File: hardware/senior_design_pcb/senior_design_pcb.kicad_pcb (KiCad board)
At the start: 4 copper layers, 15 parts, among them J8 Conn_02x08_Odd_Even, SW2 SW_Push, U1 FT232RL, U2 STM32F091RCTx, U3 LD1117S33TR_SOT223, X1 32.768kHz(12.5pF), X2 8MHz(20pF)

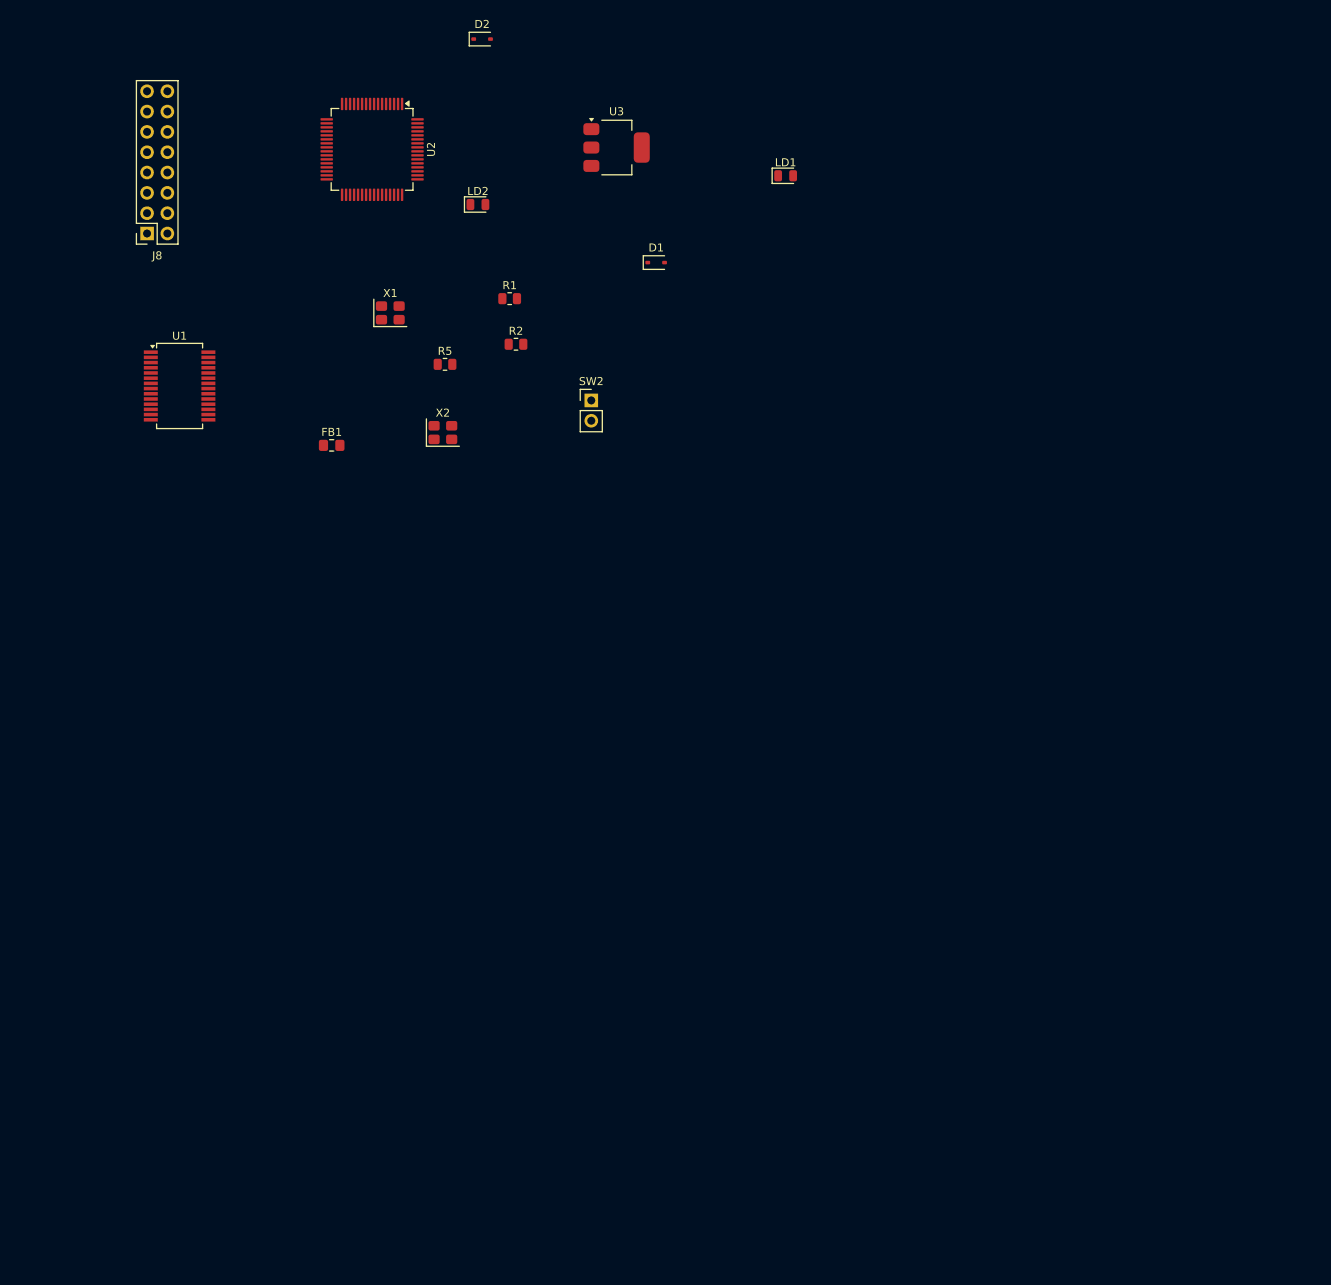
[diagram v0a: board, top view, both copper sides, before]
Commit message: added pcb, removed schematic level
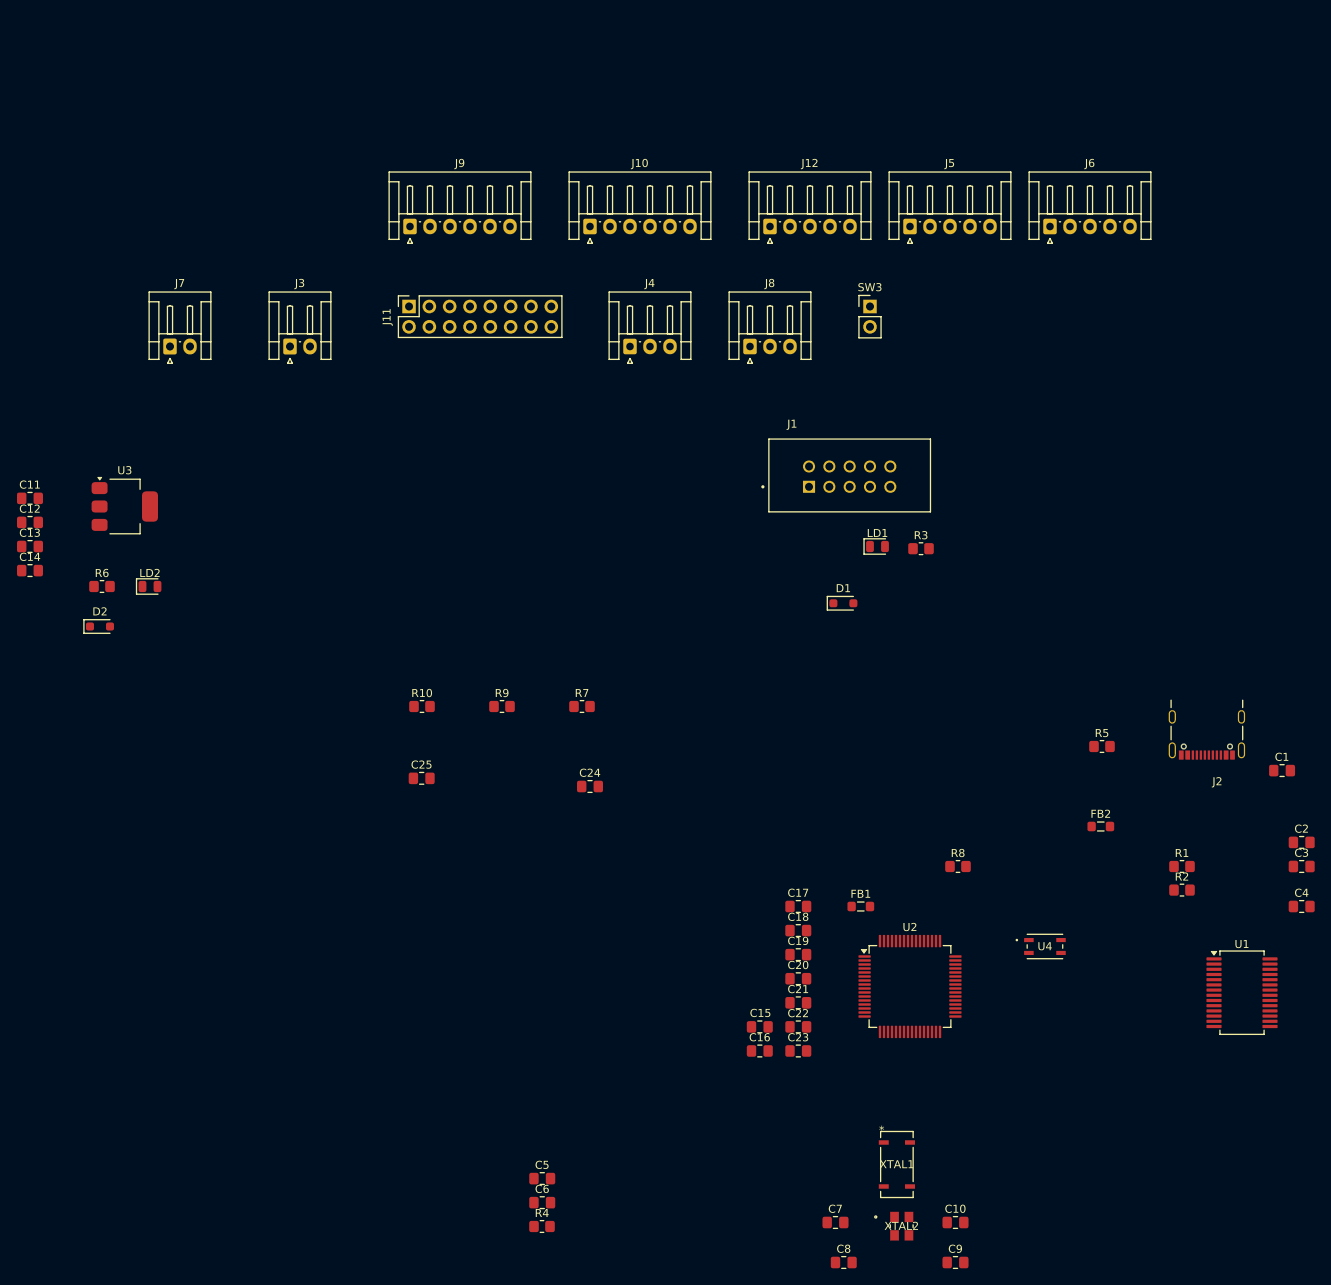
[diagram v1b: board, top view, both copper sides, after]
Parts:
- removed SW2: SW_Push, Connector_PinHeader_2.54mm:PinHeader_1x02_P2.54mm_Vertical
- removed X1: 32.768kHz(12.5pF), Crystal:Crystal_SMD_3225-4Pin_3.2x2.5mm
- removed X2: 8MHz(20pF), Crystal:Crystal_SMD_3225-4Pin_3.2x2.5mm
- added C1: 10nF, Capacitor_SMD:C_0805_2012Metric_Pad1.18x1.45mm_HandSolder, F.Cu at (191.5, 128.0)
- added C10: 22uF, Capacitor_SMD:C_0805_2012Metric_Pad1.18x1.45mm_HandSolder, F.Cu at (150.7, 184.5)
- added C11: .1uF, Capacitor_SMD:C_0805_2012Metric_Pad1.18x1.45mm_HandSolder, F.Cu at (35.0, 94.0)
- added C12: .1uF, Capacitor_SMD:C_0805_2012Metric_Pad1.18x1.45mm_HandSolder, F.Cu at (35.0, 97.0)
- added C13: .1uF, Capacitor_SMD:C_0805_2012Metric_Pad1.18x1.45mm_HandSolder, F.Cu at (35.0, 100.0)
- added C14: 4.7uf, Capacitor_SMD:C_0805_2012Metric_Pad1.18x1.45mm_HandSolder, F.Cu at (35.0, 103.0)
- added C15: .1uF, Capacitor_SMD:C_0805_2012Metric_Pad1.18x1.45mm_HandSolder, F.Cu at (126.2, 160.1)
- added C16: 4.7uf, Capacitor_SMD:C_0805_2012Metric_Pad1.18x1.45mm_HandSolder, F.Cu at (126.2, 163.1)
- added C17: 1uf, Capacitor_SMD:C_0805_2012Metric_Pad1.18x1.45mm_HandSolder, F.Cu at (131.0, 145.0)
- added C18: 10nf, Capacitor_SMD:C_0805_2012Metric_Pad1.18x1.45mm_HandSolder, F.Cu at (131.0, 148.0)
- added C19: 1uf, Capacitor_SMD:C_0805_2012Metric_Pad1.18x1.45mm_HandSolder, F.Cu at (131.0, 151.0)
- added C2: 100nF, Capacitor_SMD:C_0805_2012Metric_Pad1.18x1.45mm_HandSolder, F.Cu at (194.0, 137.0)
- added C20: 12.5pF, Capacitor_SMD:C_0805_2012Metric_Pad1.18x1.45mm_HandSolder, F.Cu at (131.0, 154.0)
- added C21: 12.5pF, Capacitor_SMD:C_0805_2012Metric_Pad1.18x1.45mm_HandSolder, F.Cu at (131.0, 157.0)
- added C22: .1uF, Capacitor_SMD:C_0805_2012Metric_Pad1.18x1.45mm_HandSolder, F.Cu at (131.0, 160.1)
- added C23: .1uF, Capacitor_SMD:C_0805_2012Metric_Pad1.18x1.45mm_HandSolder, F.Cu at (131.0, 163.1)
- added C24: .1uF, Capacitor_SMD:C_0805_2012Metric_Pad1.18x1.45mm_HandSolder, F.Cu at (105.0, 130.0)
- added C25: .1uF, Capacitor_SMD:C_0805_2012Metric_Pad1.18x1.45mm_HandSolder, F.Cu at (84.0, 129.0)
- added C3: 4.7uF, Capacitor_SMD:C_0805_2012Metric_Pad1.18x1.45mm_HandSolder, F.Cu at (194.0, 140.0)
- added C4: 100nF, Capacitor_SMD:C_0805_2012Metric_Pad1.18x1.45mm_HandSolder, F.Cu at (194.0, 145.0)
- added C5: 20pF, Capacitor_SMD:C_0805_2012Metric_Pad1.18x1.45mm_HandSolder, F.Cu at (99.0, 179.0)
- added C6: 20pF, Capacitor_SMD:C_0805_2012Metric_Pad1.18x1.45mm_HandSolder, F.Cu at (99.0, 182.0)
- added C7: 22uF, Capacitor_SMD:C_0805_2012Metric_Pad1.18x1.45mm_HandSolder, F.Cu at (135.7, 184.5)
- added C8: .1uF, Capacitor_SMD:C_0805_2012Metric_Pad1.18x1.45mm_HandSolder, F.Cu at (136.7, 189.5)
- added C9: .1uF, Capacitor_SMD:C_0805_2012Metric_Pad1.18x1.45mm_HandSolder, F.Cu at (150.7, 189.5)
- added FB2: Ferrite Bead, Inductor_SMD:L_0805_2012Metric_Pad1.05x1.20mm_HandSolder, F.Cu at (168.8, 135.0)
- added J1: SBH11-PBPC-D05-ST-BK, General Library:jtag_conn, F.Cu at (137.5, 91.3)
- added J10: Screw_Terminal_01x06, Connector_JST:JST_EH_S6B-EH_1x06_P2.50mm_Horizontal, F.Cu at (105.0, 60.0)
- added J11: Conn_02x08_Odd_Even, Connector_PinSocket_2.54mm:PinSocket_2x08_P2.54mm_Vertical, F.Cu at (82.4, 70.0)
- added J12: Conn_01x05_Socket, Connector_JST:JST_EH_S5B-EH_1x05_P2.50mm_Horizontal, F.Cu at (127.5, 60.0)
- added J2: USB_C_Receptacle_USB2.0_16P, Sr_ Design:USB-C-PORT-2, F.Cu at (182.1, 122.3)
- added J3: Conn_01x02_Socket, Connector_JST:JST_EH_S2B-EH_1x02_P2.50mm_Horizontal, F.Cu at (67.5, 75.0)
- added J4: Conn_01x03_Socket, Connector_JST:JST_EH_S3B-EH_1x03_P2.50mm_Horizontal, F.Cu at (110.0, 75.0)
- added J5: Conn_01x05_Socket, Connector_JST:JST_EH_S5B-EH_1x05_P2.50mm_Horizontal, F.Cu at (145.0, 60.0)
- added J6: Conn_01x05_Socket, Connector_JST:JST_EH_S5B-EH_1x05_P2.50mm_Horizontal, F.Cu at (162.5, 60.0)
- added J7: Conn_01x02_Socket, Connector_JST:JST_EH_S2B-EH_1x02_P2.50mm_Horizontal, F.Cu at (52.5, 75.0)
- added J9: Screw_Terminal_01x06, Connector_JST:JST_EH_S6B-EH_1x06_P2.50mm_Horizontal, F.Cu at (82.5, 60.0)
- added R10: 10K, Resistor_SMD:R_0805_2012Metric_Pad1.20x1.40mm_HandSolder, F.Cu at (84.0, 120.0)
- added R3: 5k11, Resistor_SMD:R_0805_2012Metric_Pad1.20x1.40mm_HandSolder, F.Cu at (146.4, 100.3)
- added R4: 1M, Resistor_SMD:R_0805_2012Metric_Pad1.20x1.40mm_HandSolder, F.Cu at (99.0, 185.0)
- added R6: 10K, Resistor_SMD:R_0805_2012Metric_Pad1.20x1.40mm_HandSolder, F.Cu at (44.0, 105.0)
- added R7: 100K, Resistor_SMD:R_0805_2012Metric_Pad1.20x1.40mm_HandSolder, F.Cu at (104.0, 120.0)
- added R8: 10K, Resistor_SMD:R_0805_2012Metric_Pad1.20x1.40mm_HandSolder, F.Cu at (151.0, 140.0)
- added R9: 10K, Resistor_SMD:R_0805_2012Metric_Pad1.20x1.40mm_HandSolder, F.Cu at (94.0, 120.0)
- added SW3: SW_Push, Connector_PinHeader_2.54mm:PinHeader_1x02_P2.54mm_Vertical, F.Cu at (140.0, 70.0)
- added U4: KMR241GLFS, General Library:KMR241G-RESET-BUTTON, F.Cu at (161.9, 150.0)
- added XTAL1: 32.768kHz(12.5pF), Sr_ Design:ECS - CRYSTAL 32.7680KHZ 6PF SMD, F.Cu at (143.4, 177.2)
- added XTAL2: 8MHz(8PF), Sr_ Design:ECS-CRYSTAL 8MHZ 8PF SMD, F.Cu at (144.0, 185.0)
- D1, D2: footprint Diode_SMD:D_SOD-323 -> Diode_SMD:D_SOD-323_HandSoldering
- FB1: footprint Inductor_SMD:L_0805_2012Metric_Pad1.15x1.40mm_HandSolder -> Inductor_SMD:L_0805_2012Metric_Pad1.05x1.20mm_HandSolder
- J8: value Conn_02x08_Odd_Even -> Conn_01x03_Socket; footprint Connector_PinSocket_2.54mm:PinSocket_2x08_P2.54mm_Vertical -> Connector_JST:JST_EH_S3B-EH_1x03_P2.50mm_Horizontal
- R1, R2: footprint Resistor_SMD:R_0805_2012Metric -> Resistor_SMD:R_0805_2012Metric_Pad1.20x1.40mm_HandSolder
- R5: value 1M -> 1k; footprint Resistor_SMD:R_0805_2012Metric -> Resistor_SMD:R_0805_2012Metric_Pad1.20x1.40mm_HandSolder
- moved U1 152.9 mm to (186.5, 155.8)
- moved U2 124.4 mm to (145.0, 155.0), turned to 0 degrees
- moved R1 110.0 mm to (179.0, 140.0)
- moved R2 107.6 mm to (179.0, 142.9)
- moved R5 95.0 mm to (169.0, 125.0)
- moved FB1 87.7 mm to (138.8, 145.0)
- moved D2 87.6 mm to (43.8, 110.0)
- moved J8 76.7 mm to (125.0, 75.0), turned to 0 degrees
- moved U3 76.1 mm to (46.9, 95.0)
- moved LD2 62.9 mm to (50.0, 105.0)
- moved D1 48.6 mm to (136.7, 107.1)
- moved LD1 47.7 mm to (140.9, 100.0)
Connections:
- net /stm/PC13 renamed /stm/CONTROLLER-BUTTON
- FB1 pad 1: /stm/3VA -> +5V
- FB1 pad 2: +3V0 -> /stm/VBUS
- J8 pad 1: /stm/PB11 -> +5V
- J8 pad 2: /stm/G1 -> /stm/IR_IN_2
- J8 pad 3: /stm/B1 -> GND
- R5 pad 1: Net-(J2-SHIELD) -> +3V0
- R5 pad 2: GND -> Net-(LD2-A)
- U2 pad 10: /stm/PC2 -> /stm/ADMIN_JOYSTICK-BUTTON
- U2 pad 43: /stm/ADMIN_JOYSTICK-BUTTON -> /stm/PA10
- U2 pad 44: /stm/ADMIN_JOYSTICK-Y -> /stm/PA11
- U2 pad 45: /stm/ADMIN_JOYSTICK-X -> /stm/PA12
- U2 pad 8: /stm/PC0 -> /stm/ADMIN_JOYSTICK-X
- U2 pad 9: /stm/PC1 -> /stm/ADMIN_JOYSTICK-Y
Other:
- board text added: "the connectors are all 2.5 NOT 2.56mm rn"

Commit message: organized components
added labels
grouped
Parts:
- removed J2: USB_C_Receptacle_USB2.0_16P, Sr_ Design:USB-C-PORT-2
- removed U1: FT232RL, Package_SO:SSOP-28_5.3x10.2mm_P0.65mm
- added FT1: ~, Package_SO:SSOP-28_5.3x10.2mm_P0.65mm, F.Cu at (201.5, 102.7)
- added J13: UJ20-C-H-C-4-SMT-TR, Sr_ Design:USB-C-PORT-2, F.Cu at (200.7, 86.0)
- J10: value Screw_Terminal_01x06 -> 1x06Screw-Stepper Driver2
- J11: value Conn_02x08_Odd_Even -> 2x08Rectangle-LED Matrix Connector
- J12: value Conn_01x05_Socket -> 1x05JST - Joystick2 connector
- J3, J7: value Conn_01x02_Socket -> 1x02JST-IR Transmitter
- J4: value Conn_01x03_Socket -> 1x03JST- IR Receiver
- J5: value Conn_01x05_Socket -> 1x05JST-Admin LCD Console Connector
- J6: value Conn_01x05_Socket -> 1x05JST - Joystick1 connector
- J8: value Conn_01x03_Socket -> 1x03JST-IR Receiver
- J9: value Screw_Terminal_01x06 -> 1x06Screw-Stepper Driver
- SW3: value SW_Push -> 1x02JST-Admin Console button connector
- moved R6 224.7 mm to (266.0, 70.0)
- moved C24 186.2 mm to (268.0, 40.0)
- moved R9 174.2 mm to (246.0, 35.0)
- moved C23 164.8 mm to (246.0, 45.0)
- moved C25 162.9 mm to (223.0, 44.0)
- moved R10 162.9 mm to (223.0, 35.0)
- moved C22 156.0 mm to (265.0, 80.0)
- moved R8 155.7 mm to (266.0, 35.0)
- moved R4 145.0 mm to (199.0, 80.0)
- moved SW3 126.2 mm to (265.0, 52.5)
- moved U4 122.4 mm to (258.0, 74.2)
- moved C10 120.4 mm to (49.0, 120.0)
- moved C7 120.4 mm to (34.0, 120.0)
- moved C8 120.4 mm to (35.0, 125.0)
- moved C9 120.4 mm to (49.0, 125.0)
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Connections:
- net /stm/3VA renamed /3VA
- net /stm/A renamed /A
- net /stm/ADMIN_CONSOLE-BUTTON renamed /ADMIN_CONSOLE-BUTTON
- net /stm/ADMIN_JOYSTICK-BUTTON renamed /ADMIN_JOYSTICK-BUTTON
- net /stm/ADMIN_JOYSTICK-X renamed /ADMIN_JOYSTICK-X
- net /stm/ADMIN_JOYSTICK-Y renamed /ADMIN_JOYSTICK-Y
- net /stm/B renamed /B
- net /stm/B1 renamed /B1
- net /stm/B2 renamed /B2
- net /stm/BOOT0 renamed /BOOT0
- net /stm/C renamed /C
- net /stm/CLK renamed /CLK
- net /stm/CONSOLE_DISP-1 renamed /CONSOLE_DISP-1
- net /stm/CONSOLE_DISP-2 renamed /CONSOLE_DISP-2
- net /stm/CONSOLE_DISP-3 renamed /CONSOLE_DISP-3
- net /stm/CONTROLLER-BUTTON renamed /CONTROLLER-BUTTON
- net /stm/CONTROLLER_X_IN renamed /CONTROLLER_X_IN
- net /stm/CONTROLLER_Y_IN renamed /CONTROLLER_Y_IN
- net /stm/D renamed /D
- net /stm/G1 renamed /G1
- net /stm/G2 renamed /G2
- net /stm/HS_CLK-IN renamed /HS_CLK-IN
- net /stm/HS_CLK-OUT renamed /HS_CLK-OUT
- net /stm/IR_IN_1 renamed /IR_IN_1
- net /stm/IR_IN_2 renamed /IR_IN_2
- net /stm/LAT renamed /LAT
- net /stm/LS_CLK-IN renamed /LS_CLK-IN
- net /stm/LS_CLK-OUT renamed /LS_CLK-OUT
- net /stm/NRST renamed /NRST
- net /stm/OE renamed /OE
- net /stm/PA10 renamed /PA10
- net /stm/PA11 renamed /PA11
- net /stm/PA12 renamed /PA12
- net /stm/PA13 renamed /PA13
- net /stm/PA14 renamed /PA14
- net /stm/PB1 renamed /PB1
- net /stm/PB11 renamed /PB11
- net /stm/PB12 renamed /PB12
- net /stm/PB13 renamed /PB13
- net /stm/PB14 renamed /PB14
- net /stm/PB15 renamed /PB15
- net /stm/PB4 renamed /PB4
- net /stm/PB5 renamed /PB5
- net /stm/PB6 renamed /PB6
- net /stm/PB7 renamed /PB7
- net /stm/PB8 renamed /PB8
- net /stm/PB9 renamed /PB9
- net /stm/PC3 renamed /PC3
- net /stm/PC6 renamed /PC6
- net /stm/PC7 renamed /PC7
- net /stm/PC8 renamed /PC8
- net /stm/PC9 renamed /PC9
- net /stm/U5V renamed /U5V
- net /stm/USER_JOYSTICK-BUTTON renamed /USER_JOYSTICK-BUTTON
- net /stm/USER_JOYSTICK-X renamed /USER_JOYSTICK-X
- net /stm/USER_JOYSTICK-Y renamed /USER_JOYSTICK-Y
- net /stm/V3.3_IN renamed /V3.3_IN
- net /stm/VBUS renamed /VBUS
- U2 pad 53: /stm/PC12 -> /PC12
- U2 pad 54: /stm/PD2 -> /PD2

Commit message: edited layout
made it more finalized, some changes needed still.
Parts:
- C1: value 10nF -> .01uF
- C18: value 10nf -> .01uF
- C2, C4: value 100nF -> .1uF
- J12: value 1x05JST - Joystick2 connector -> 1x05JST - Joystick2 connector (gamer)
- J3: value 1x02JST-IR Transmitter -> 1x02JST-IR Transmitter1
- J4: value 1x03JST- IR Receiver -> 1x03JST- IR Receiver1
- J6: value 1x05JST - Joystick1 connector -> 1x05JST - Joystick1 connector (admin)
- J8: value 1x03JST-IR Receiver -> 1x03JST-IR Receiver2
- moved C3 194.1 mm to (31.0, 69.0)
- moved C1 186.1 mm to (34.0, 74.5), turned to 90 degrees
- moved J13 178.7 mm to (22.1, 79.4), turned to -90 degrees
- moved R4 175.7 mm to (23.4, 86.9)
- moved C2 168.3 mm to (54.1, 86.0)
- moved C22 164.3 mm to (100.7, 83.3), turned to -90 degrees
- moved C4 157.6 mm to (38.7, 82.8), turned to -90 degrees
- moved R6 156.8 mm to (109.9, 84.8), turned to -90 degrees
- moved FT1 156.4 mm to (46.2, 83.7), turned to 180 degrees
- moved R2 155.2 mm to (32.2, 82.3), turned to -45 degrees
- moved U4 152.3 mm to (105.7, 78.9), turned to -90 degrees
- moved R8 151.5 mm to (126.1, 93.0), turned to 180 degrees
- moved R1 151.1 mm to (36.5, 78.0)
- moved C24 150.5 mm to (126.0, 89.8)
- moved FB1 149.2 mm to (30.0, 74.5), turned to -90 degrees
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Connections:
- net Net-(D2-A) renamed /3v3-vo
- C25 pad 2: /USER_JOYSTICK-BUTTON -> /PC13
- J12 pad 2: /USER_JOYSTICK-BUTTON -> /PC13
- J12 pad 3: /USER_JOYSTICK-X -> /PA0
- J12 pad 4: /USER_JOYSTICK-Y -> /PA1
- R10 pad 1: /USER_JOYSTICK-BUTTON -> /PC13
- U2 pad 14: /CONTROLLER_X_IN -> /PA0
- U2 pad 15: /CONTROLLER_Y_IN -> /PA1
- U2 pad 2: /CONTROLLER-BUTTON -> /PC13
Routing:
- added copper zone on F.Cu, net GND

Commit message: cleaned it up
added comments and added squares.
reorganized into more precise rectangles
marked extra requirements
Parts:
- moved R8 12.4 mm to (137.5, 97.8)
- moved J5 12.4 mm to (128.9, 100.3)
- moved C10 12.4 mm to (61.5, 53.3)
- moved C12 12.4 mm to (117.5, 72.1)
- moved C13 12.4 mm to (110.3, 51.8)
- moved C14 12.4 mm to (75.0, 53.2)
- moved C18 12.4 mm to (117.9, 56.4)
- moved C19 12.4 mm to (119.9, 59.7)
- moved C24 12.4 mm to (137.4, 94.6)
- moved C7 12.4 mm to (55.8, 68.1)
- moved FB2 12.4 mm to (81.0, 60.5)
- moved J10 12.4 mm to (82.7, 99.8)
- moved J11 12.4 mm to (113.9, 34.5)
- moved J4 12.4 mm to (84.1, 39.5)
- moved J7 12.4 mm to (69.1, 39.8)
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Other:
- board outline added: 290 x 202.5 mm
- board text added: "common gnd for tehse"
